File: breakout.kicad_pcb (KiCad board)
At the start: 2 copper layers, 50 x 50 mm, 38 parts, among them J1 JACK_TRS_4PINS, P1 CONN_01X08, P2 SPEAKER, P3 ISO7816_SIMPLE, P4 CONN_01X09, P5 SMA_CONN, P6 MIC, P7 USB_OTG, Q1 Q_PMOS_GSD, Q2 Q_NMOS_GSD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

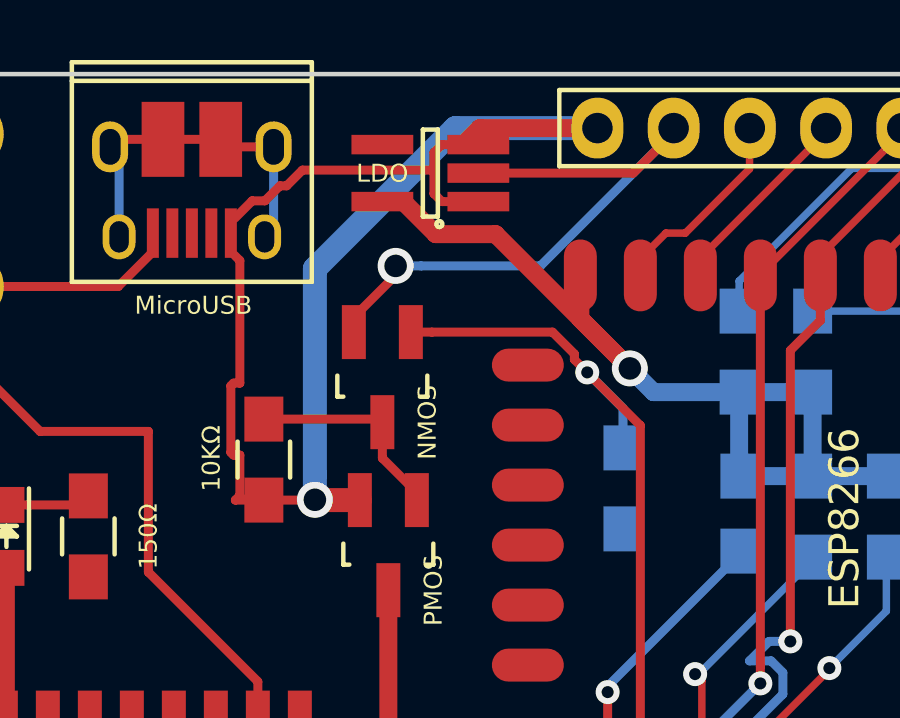
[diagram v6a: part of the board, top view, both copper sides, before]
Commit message: Increase the Vcc bus width.
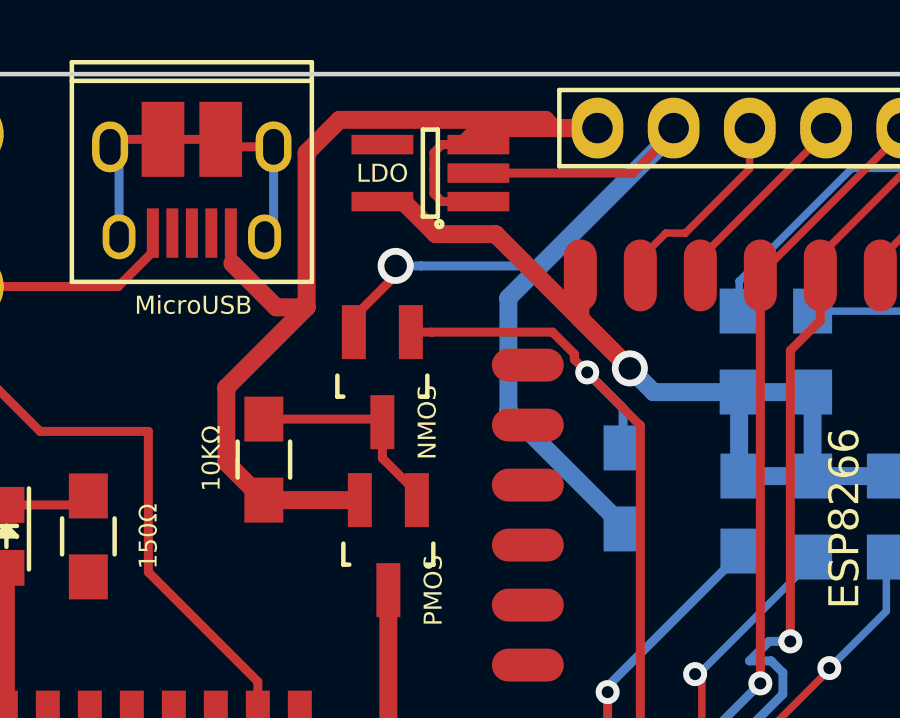
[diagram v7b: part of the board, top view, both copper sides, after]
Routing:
- net GND: track 62.1 -> 79.2 mm
- net /Vcc: track 49.3 -> 39.3 mm, vias 1 -> 0
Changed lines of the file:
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@@
     (links 105)
     (no_connects 0)
-    (area 149.924999 49.924999 200.075001 100.075001)
+    (area 148.052858 46.55 204.515 100.425001)
     (thickness 1.6)
     (drawings 53)
-    (tracks 367)
+    (tracks 361)
     (zones 0)
     (modules 38)
@@
   )
   (setup
-    (last_trace_width 0.3)
+    (last_trace_width 0.6)
     (user_trace_width 0.3)
     (user_trace_width 0.6)
@@
   (gr_line (start 200 52.2) (end 200 97.8) (layer Edge.Cuts) (width 0.15))
   (gr_line (start 152.2 50) (end 197.8 50) (layer Edge.Cuts) (width 0.15))
+  (segment (start 174.95 57.4624) (end 174.95 61.237) (width 0.6) (layer B.Cu) (net 1))
+  (segment (start 174.95 61.237) (end 178.772 65.059) (width 0.6) (layer B.Cu) (net 1))
+  (segment (start 178.772 65.059) (end 178.772 65.159) (width 0.6) (layer B.Cu) (net 1))
+  (segment (start 180.46 51.9524) (end 174.95 57.4624) (width 0.6) (layer B.Cu) (net 1))
   (segment (start 171.192762 56.706858) (end 171.192762 56.393762) (width 0.3) (layer F.Cu) (net 1))
   (segment (start 169.8 58.6) (end 169.8 58.09962) (width 0.3) (layer F.Cu) (net 1))
@@
   (segment (start 185.53 51.9524) (end 181.4 56.0824) (width 0.25) (layer F.Cu) (net 38) (status 30))
   (segment (start 181.4 56.0824) (end 181.4 56.75) (width 0.25) (layer F.Cu) (net 38) (status 30))
-  (segment (start 168.511339 64.2) (end 168.501575 64.190236) (width 0.8) (layer F.Cu) (net 39))
-  (segment (start 170 64.2) (end 168.511339 64.2) (width 0.8) (layer F.Cu) (net 39))
-  (segment (start 168.501575 63.341708) (end 168.501575 64.190236) (width 0.8) (layer B.Cu) (net 39))
-  (segment (start 168.501575 56.484653) (end 168.501575 63.341708) (width 0.8) (layer B.Cu) (net 39))
-  (segment (start 173.186228 51.8) (end 168.501575 56.484653) (width 0.8) (layer B.Cu) (net 39))
-  (segment (start 177.92 51.8) (end 173.186228 51.8) (width 0.8) (layer B.Cu) (net 39))
-  (via (at 168.501575 64.190236) (size 1.2) (drill 0.75) (layers F.Cu B.Cu) (net 39))
-  (segment (start 166.8 64.2) (end 170 64.2) (width 0.3) (layer F.Cu) (net 39) (status 30))
-  (segment (start 165.82499 54.810783) (end 166.410783 54.22499) (width 0.3) (layer F.Cu) (net 39) (status 10))
-  (segment (start 166.8 64.2) (end 165.85 64.2) (width 0.3) (layer F.Cu) (net 39) (status 10))
-  (segment (start 166 60.299999) (end 166 56.214227) (width 0.3) (layer F.Cu) (net 39))
-  (segment (start 165.699999 60.389999) (end 165.789999 60.299999) (width 0.3) (layer F.Cu) (net 39))
-  (segment (start 165.699999 62.610001) (end 165.699999 60.389999) (width 0.3) (layer F.Cu) (net 39))
-  (segment (start 165.789999 60.299999) (end 166 60.299999) (width 0.3) (layer F.Cu) (net 39))
-  (segment (start 165.789999 62.700001) (end 165.699999 62.610001) (width 0.3) (layer F.Cu) (net 39))
-  (segment (start 166 62.700001) (end 165.789999 62.700001) (width 0.3) (layer F.Cu) (net 39))
-  (segment (start 166 64.05) (end 166 62.700001) (width 0.3) (layer F.Cu) (net 39))
-  (segment (start 166 56.214227) (end 165.82499 56.039217) (width 0.3) (layer F.Cu) (net 39) (status 20))
-  (segment (start 165.85 64.2) (end 166 64.05) (width 0.3) (layer F.Cu) (net 39))
-  (segment (start 166.410783 54.22499) (end 166.83501 54.22499) (width 0.3) (layer F.Cu) (net 39))
-  (segment (start 166.83501 54.22499) (end 167.33499 53.72501) (width 0.3) (layer F.Cu) (net 39))
-  (segment (start 167.33499 53.72501) (end 167.559928 53.72501) (width 0.3) (layer F.Cu) (net 39))
-  (segment (start 167.559928 53.72501) (end 168.084938 53.2) (width 0.3) (layer F.Cu) (net 39))
-  (segment (start 168.084938 53.2) (end 172.469999 53.2) (width 0.3) (layer F.Cu) (net 39))
+  (segment (start 165.7 55.3) (end 165.7 56.26) (width 0.3) (layer F.Cu) (net 39))
+  (segment (start 165.7 56.26) (end 165.750001 56.310001) (width 0.3) (layer F.Cu) (net 39))
+  (segment (start 166.8 64.2) (end 170 64.2) (width 0.6) (layer F.Cu) (net 39))
+  (segment (start 167.214988 57.774988) (end 165.750001 56.310001) (width 0.6) (layer F.Cu) (net 39))
+  (segment (start 168.22501 57.774988) (end 167.214988 57.774988) (width 0.6) (layer F.Cu) (net 39))
+  (segment (start 177.92 51.8) (end 176.4564 51.8) (width 0.6) (layer F.Cu) (net 39))
+  (segment (start 176.4564 51.8) (end 176.181399 51.524999) (width 0.6) (layer F.Cu) (net 39))
+  (segment (start 176.181399 51.524999) (end 169.319999 51.524999) (width 0.6) (layer F.Cu) (net 39))
+  (segment (start 168.22501 52.619988) (end 168.22501 57.774988) (width 0.6) (layer F.Cu) (net 39))
+  (segment (start 169.319999 51.524999) (end 168.22501 52.619988) (width 0.6) (layer F.Cu) (net 39))
+  (segment (start 168.22501 57.774988) (end 165.55 60.449998) (width 0.6) (layer F.Cu) (net 39))
+  (segment (start 165.55 60.449998) (end 165.55 62.95) (width 0.6) (layer F.Cu) (net 39))
+  (segment (start 165.55 62.95) (end 166.8 64.2) (width 0.6) (layer F.Cu) (net 39))
+  (segment (start 172.734998 52.35) (end 173.45 52.35) (width 0.3) (layer F.Cu) (net 39) (status 20))
+  (segment (start 172.469999 52.614999) (end 172.734998 52.35) (width 0.3) (layer F.Cu) (net 39))
+  (segment (start 172.734998 54.25) (end 172.469999 53.985001) (width 0.3) (layer F.Cu) (net 39))
+  (segment (start 166.809764 64.190236) (end 166.8 64.2) (width 0.6) (layer F.Cu) (net 39))
+  (segment (start 172.469999 53.2) (end 172.469999 52.614999) (width 0.3) (layer F.Cu) (net 39))
+  (segment (start 174 51.8) (end 173.45 52.35) (width 0.6) (layer F.Cu) (net 39) (status 20))
+  (segment (start 173.45 54.25) (end 172.734998 54.25) (width 0.3) (layer F.Cu) (net 39) (status 10))
+  (segment (start 173.45 52.35) (end 173.185002 52.35) (width 0.6) (layer F.Cu) (net 39) (status 30))
   (segment (start 177.92 51.8) (end 174 51.8) (width 0.6) (layer F.Cu) (net 39) (status 10))
-  (segment (start 174 51.8) (end 173.45 52.35) (width 0.6) (layer F.Cu) (net 39) (status 20))
   (segment (start 172.469999 53.985001) (end 172.469999 53.2) (width 0.3) (layer F.Cu) (net 39))
-  (segment (start 172.469999 53.2) (end 172.469999 52.614999) (width 0.3) (layer F.Cu) (net 39))
-  (segment (start 173.45 52.35) (end 173.185002 52.35) (width 0.6) (layer F.Cu) (net 39) (status 30))
-  (segment (start 173.45 54.25) (end 172.734998 54.25) (width 0.3) (layer F.Cu) (net 39) (status 10))
-  (segment (start 172.734998 54.25) (end 172.469999 53.985001) (width 0.3) (layer F.Cu) (net 39))
-  (segment (start 172.469999 52.614999) (end 172.734998 52.35) (width 0.3) (layer F.Cu) (net 39))
-  (segment (start 172.734998 52.35) (end 173.45 52.35) (width 0.3) (layer F.Cu) (net 39) (status 20))
   (zone (net 0) (net_name "") (layer F.Cu) (hatch full 0.508)
     (connect_pads (clearance 0.508))
